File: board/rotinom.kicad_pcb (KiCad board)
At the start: 4 copper layers, 127 x 88.9 mm, 114 parts, among them J1 Conn_01x04, J2 Conn_01x04, J3 Conn_01x02, J4 Styx_P4, J5 Styx_P5, J6 Conn_02x12_Odd_Even, P1 test_connector, Q1 MMBT2369, Q10 MMBT2369, Q11 MMBT2369, Q12 MMBT2369, Q13 MMBT2369, Q14 MMBT2369, Q15 MMBT2369, Q16 MMBT2369, Q17 MMBT2369, Q18 MMBT2369, Q19 MMBT2369, Q2 MMBT2369, Q20 MMBT2369, Q21 MMBT2369, Q22 MMBT2369, Q23 MMBT2369, Q24 MMBT2369, Q25 MMBT2369, Q26 MMBT2369, Q27 MMBT2369, Q28 MMBT2369, Q29 MMBT2369, Q3 MMBT2369, Q30 MMBT2369, Q31 MMBT2369, Q32 MMBT2369, Q33 MMBT2369, Q4 MMBT2369, Q5 MMBT2369, Q6 MMBT2369, Q7 MMBT2369, Q8 MMBT2369, Q9 MMBT2369

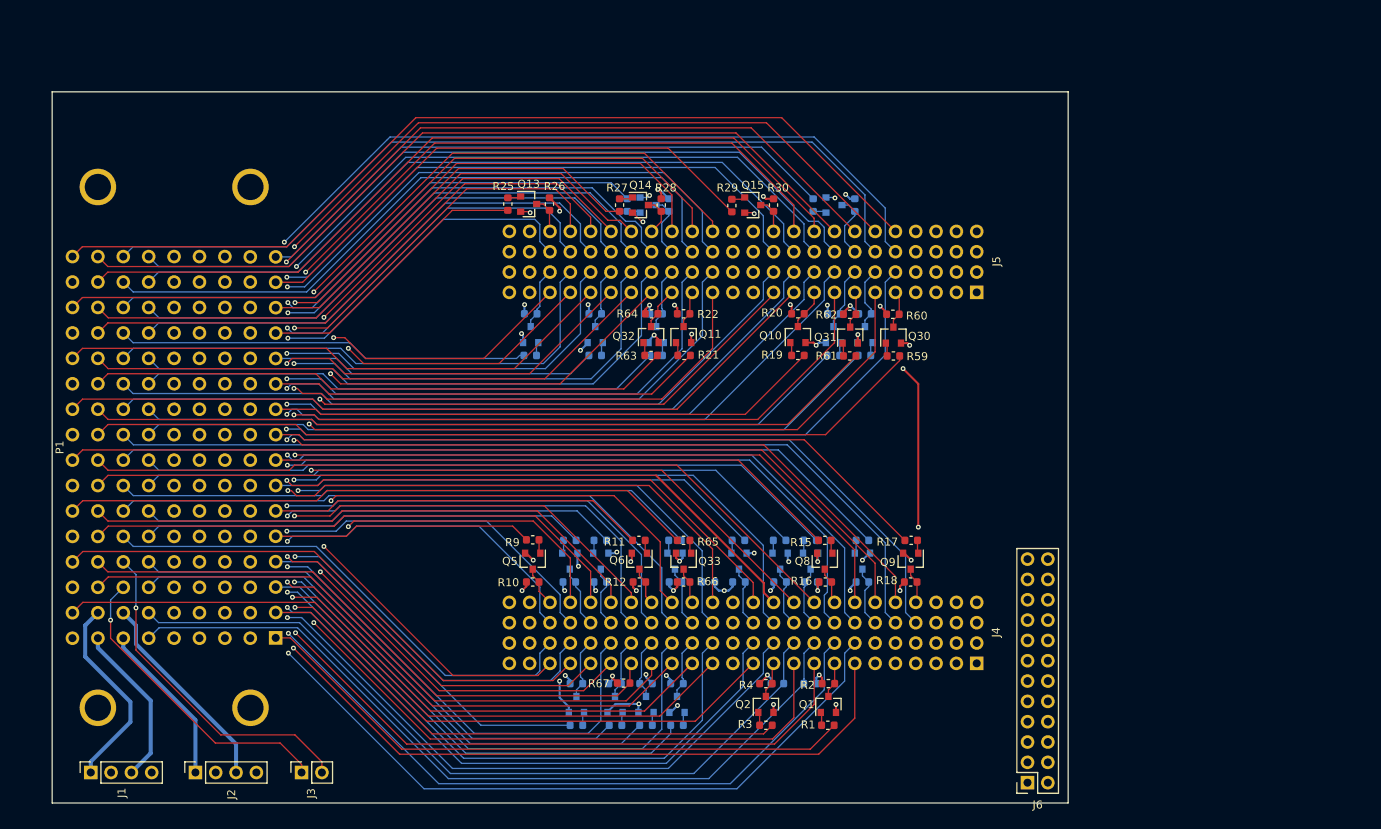
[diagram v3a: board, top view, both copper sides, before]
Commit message: Board: finished routing of extended board
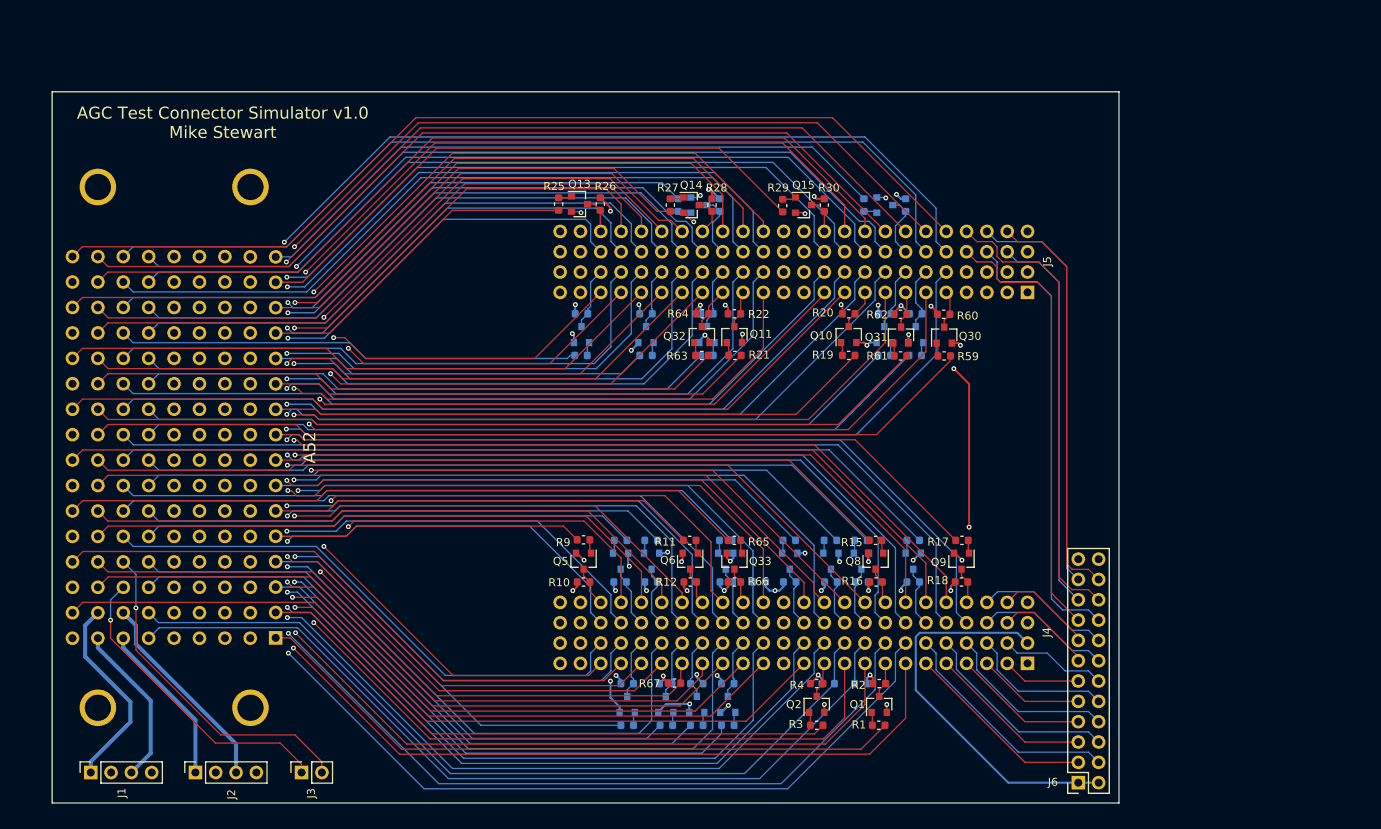
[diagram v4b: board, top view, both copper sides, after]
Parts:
- moved Q17 6.35 mm to (141.5, 133.7)
- moved Q24 6.35 mm to (165.0, 87.5)
- moved R33 6.35 mm to (141.5, 136.3)
- moved R34 6.35 mm to (141.5, 131.1)
- moved R35 6.35 mm to (137.7, 136.3)
- moved R39 6.35 mm to (135.8, 113.2)
- moved R40 6.35 mm to (135.8, 118.4)
- moved R47 6.35 mm to (165.0, 90.1)
- moved R64 6.35 mm to (142.2, 84.9)
- moved Q13 6.35 mm to (126.9, 71.2)
- moved Q19 6.35 mm to (132.0, 115.8)
- moved Q4 6.35 mm to (132.8, 133.7)
- moved R37 6.35 mm to (132.0, 113.2)
- moved R38 6.35 mm to (132.0, 118.4)
- moved R55 6.35 mm to (127.1, 90.1)
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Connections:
- J4 pad 10: /StyxConnector/DBG7 -> /StyxConnector/DBG8
- J4 pad 11: /StyxConnector/DBG10 -> /StyxConnector/DBG12
- J4 pad 12: /StyxConnector/DBG12 -> /StyxConnector/DBG14
- J4 pad 13: /StyxConnector/DBG1 -> /StyxConnector/DBG5
- J4 pad 14: /StyxConnector/DBG5 -> /StyxConnector/DBG6
- J4 pad 17: /StyxConnector/DBG2 -> /StyxConnector/DBG3
- J4 pad 18: /StyxConnector/DBG11 -> /StyxConnector/DBG4
- J4 pad 21: /StyxConnector/DBG14 -> /StyxConnector/DBG1
- J4 pad 22: /StyxConnector/DBG13 -> /StyxConnector/DBG2
- J4 pad 5: /StyxConnector/DBG3 -> /StyxConnector/DBG9
- J4 pad 6: /StyxConnector/DBG6 -> /StyxConnector/DBG10
- J4 pad 7: /StyxConnector/DBG8 -> /StyxConnector/DBG11
- J4 pad 8: /StyxConnector/DBG9 -> /StyxConnector/DBG13
- J4 pad 9: /StyxConnector/DBG4 -> /StyxConnector/DBG7
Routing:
- net /StyxConnector/DBG18: track 0.00 -> 57.9 mm
- net /StyxConnector/DBG16: track 0.00 -> 56.4 mm
- net /StyxConnector/DBG15: track 0.00 -> 55.7 mm
- net /StyxConnector/DBG19: track 0.00 -> 51.5 mm
- net /StyxConnector/DBG20: track 0.00 -> 51.2 mm
- net /StyxConnector/DBG_3V3: track 0.00 -> 49.0 mm
- net /StyxConnector/DBG17: track 0.00 -> 48.7 mm
- net /StyxConnector/DBG2: track 0.00 -> 29.0 mm
- net /StyxConnector/DBG4: track 0.00 -> 25.4 mm
- net /StyxConnector/DBG1: track 0.00 -> 24.2 mm
- net /StyxConnector/DBG6: track 0.00 -> 21.8 mm
- net /StyxConnector/DBG3: track 0.00 -> 20.6 mm
- net /StyxConnector/DBG8: track 0.00 -> 18.2 mm
- net /StyxConnector/DBG14: track 0.00 -> 17.1 mm
- net /StyxConnector/DBG12: track 0.00 -> 17.0 mm
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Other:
- board size 127 x 88.9 mm -> 133.3 x 88.9 mm
- board text added: "A52"
- board text added: "AGC Test Connector Simulator v1.0 Mike Stewart"
